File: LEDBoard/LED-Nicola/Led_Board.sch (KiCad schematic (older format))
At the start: 29 parts, among them J1 MOUNTING_HOLE, J10 CONN_01X02, J11 CONN_01X16, J12 CONN_01X02, J2 MOUNTING_HOLE, J3 MOUNTING_HOLE, J4 MOUNTING_HOLE, J5 CONN_01X04, J6 CONN_01X04, J7 CONN_01X02, J8 CONN_01X02, J9 CONN_01X02, Q1 MMBT2222ALT1G, U1 SSR

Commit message: Added changes as per Chris requests
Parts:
- removed J7: CONN_01X02, hyperCustom:CONN_PHOENIX_1844210_2PIN, symbol CONN_01X02
- added J13: LED CONN 01X04, hyperCustom:CONN_PHOENIX_1844236_4PIN, symbol CONN_01X04
- added J7: Arduino CONN_01X06, hyperCustom:CONN_PHOENIX_1844252_6PIN, symbol CONN_01X06
- added R15, R16, R17: 220, Resistors_SMD:R_1206_HandSoldering, symbol R
- J11: value CONN_01X16 -> LED CONN 01X16
- J5: value CONN_01X04 -> Arduino CONN 01X04
- J6: value CONN_01X04 -> Arduino CONN_01X04
- J8: value CONN_01X02 -> VD 0 CONN_01X02
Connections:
- net 24V: now also J5.3 (P3), U1.4 (SUPPLY2), U1.6 (SUPPLY1); no longer U1.1 (IN+)
- net A0: now also J5.2 (P2); no longer J5.4 (P4)
- net A1: now also J5.1 (P1); no longer J5.3 (P3)
- net A2: now also J6.4 (P4); no longer J5.2 (P2)
- net A3: now also J6.3 (P3); no longer J5.1 (P1)
- net A4: now also J6.2 (P2); no longer J6.4 (P4)
- net A5: now also J6.1 (P1); no longer J6.3 (P3)
- net A6: now also J7.6 (P6); no longer J6.2 (P2)
- net A7: now also J7.5 (P5), R15.2; no longer J6.1 (P1)
- net GND: now also J11.16 (P16), J13.2 (P2), J13.4 (P4), J7.2 (P2); no longer U1.2 (IN-)
- net Buzzer: now reaches U1.5 (LOAD)
- net Buzzer: now also J12.1 (P1)
- net L7: now reaches J11.15 (P15)
- net L7: now also R15.1
- net Collector: no longer names the net of Q1.3 (C)
- net Collector: now also U1.2 (IN-); no longer U1.6 (SUPPLY1)
- net LEDO renamed VDO0
- removed net buzzer: J12.1 (P1), U1.4 (SUPPLY2)
- new net 5V0: J5.4 (P4), U1.1 (IN+)
- new net A8: J7.4 (P4), R16.2
- new net A9: J7.3 (P3), R17.2
- new net L8: J13.1 (P1), R16.1
- new net L9: J13.3 (P3), R17.1
- no-connect marks 6 -> 3
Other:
- moved on the sheet: D1, J10, J11, J5, J6, J8, J9, Q1, R1, R10, R11, R12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

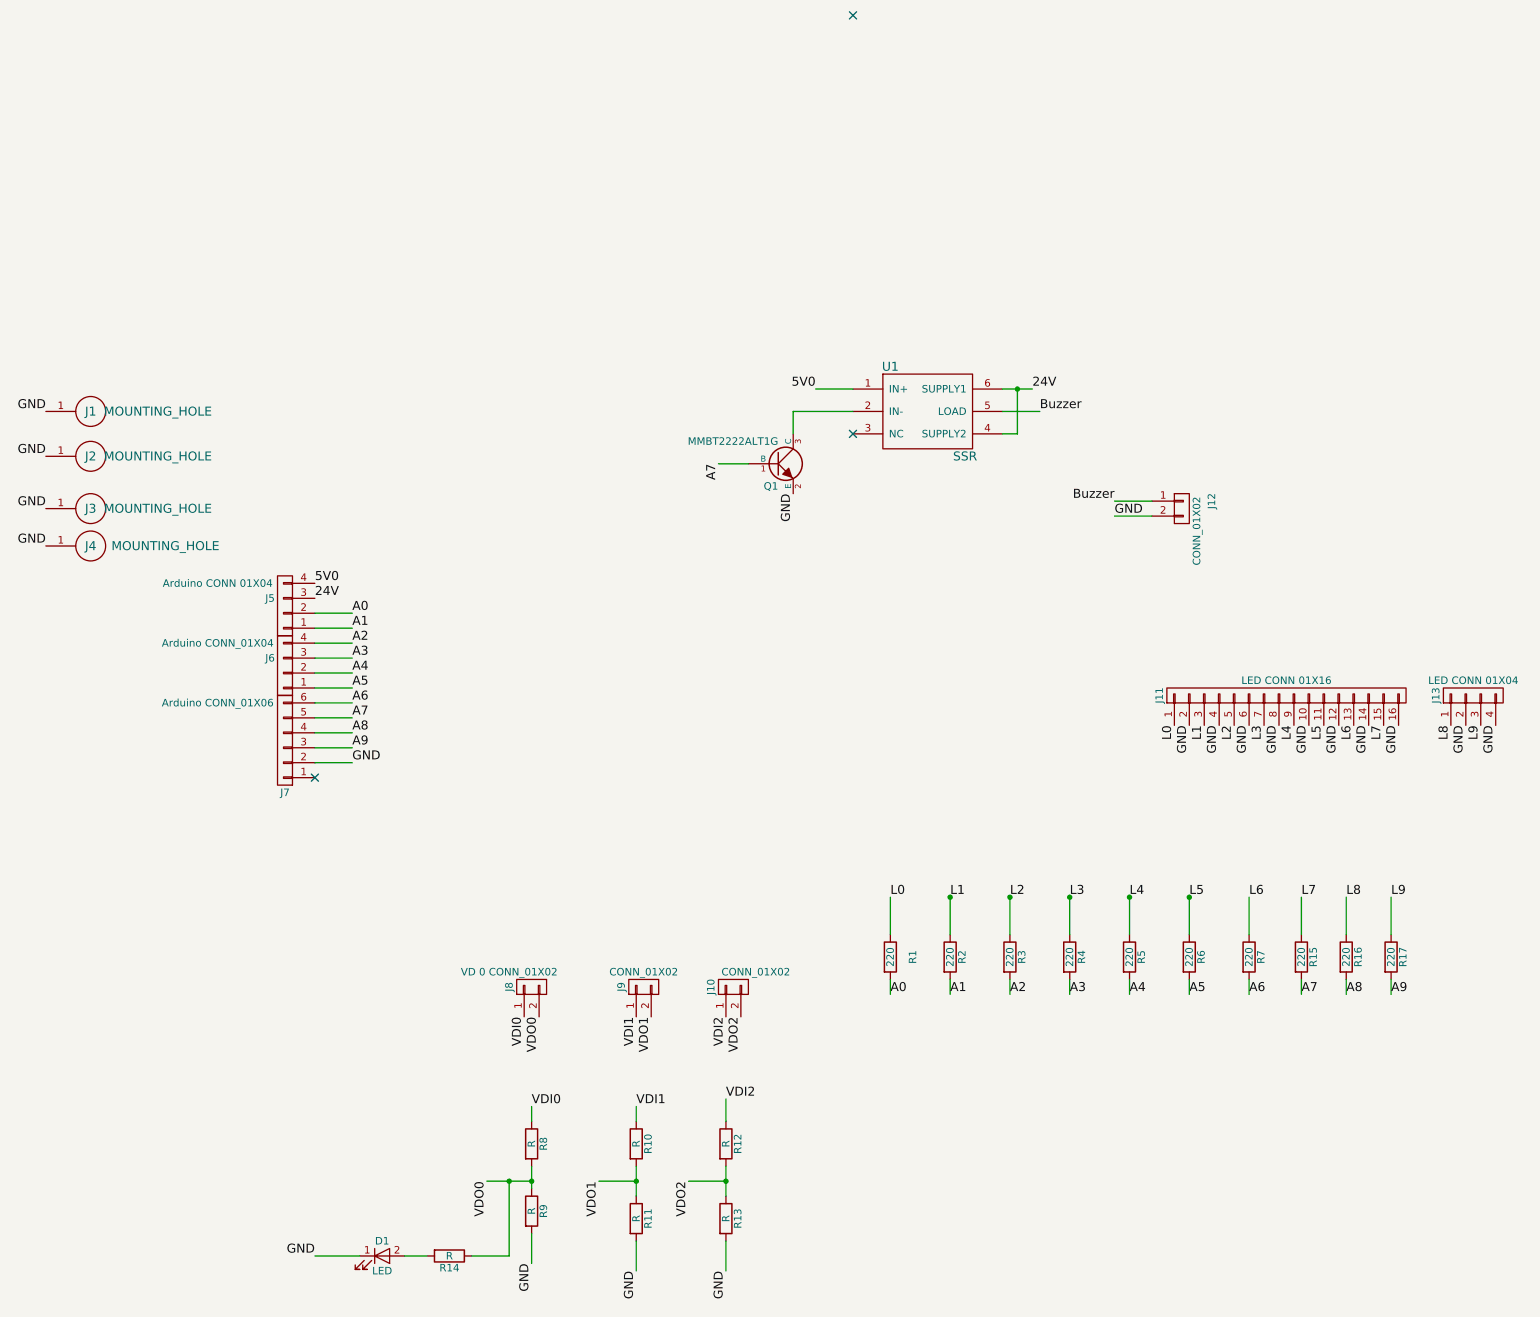
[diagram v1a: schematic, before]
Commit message: Added Digikey PN and Mfg. PN
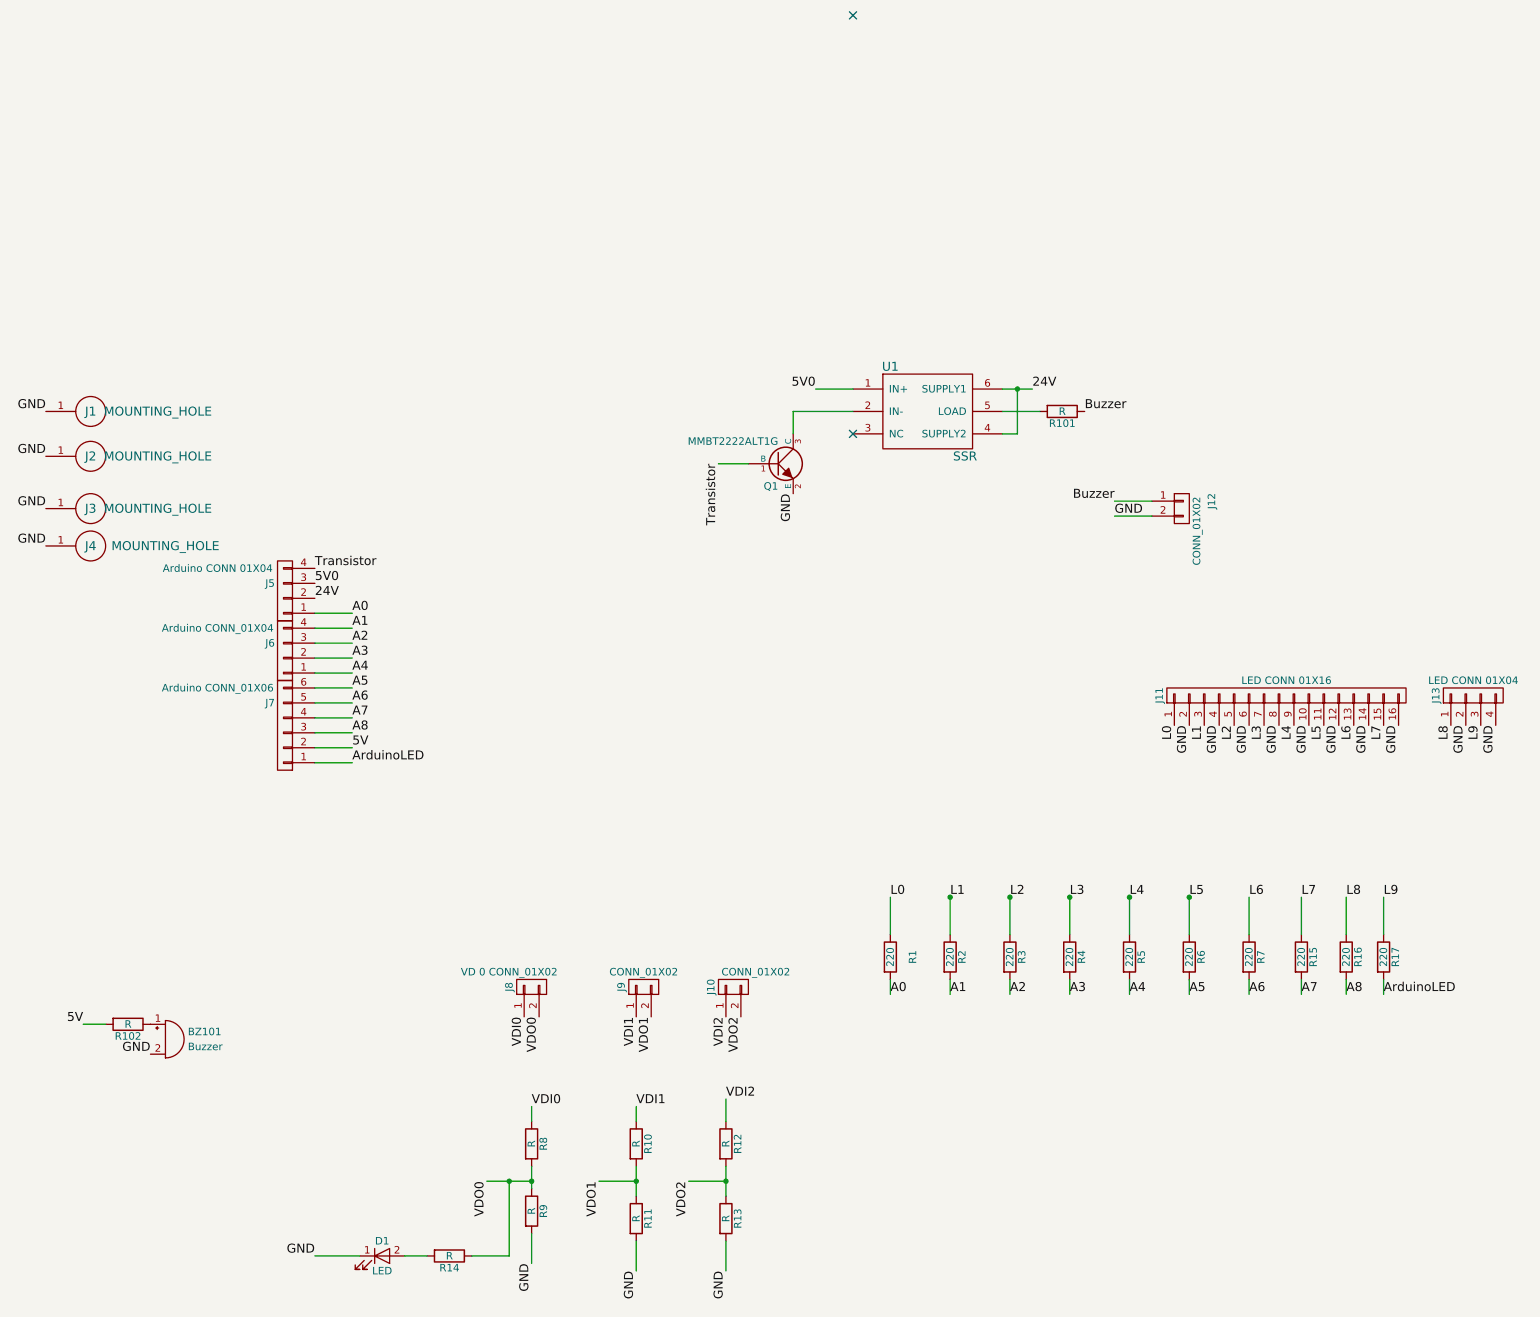
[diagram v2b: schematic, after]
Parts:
- added BZ101: Buzzer, hyperCustom:nicolaBuzzer, symbol Buzzer
- added R101, R102: R, Resistors_ThroughHole:R_Axial_DIN0309_L9.0mm_D3.2mm_P12.70mm_Horizontal, symbol R
- J10: DigiKey PN (none) -> 277-2416-ND; Mfg.  (none) -> Phoenix; Mfg. PN (none) -> 1844210
- J11: Digikey PN (none) -> 277-6211-ND; Link (none) -> https://www.digikey.com/product-detail/en/phoenix-contact/1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; Mfg.  (none) -> Phoenix; Mfg. PN (none) -> 1828003
- J12: Digikey PN (none) -> 277-2416-ND; Mfg.  (none) -> Phoenix; Mfg. PN (none) -> 1844210
- J13, J5, J6: Digikey PN (none) -> 277-2419-ND; Mfg.  (none) -> Phoenix; Mfg. PN (none) -> 1844236
- J7: Digikey PN (none) -> 277-2427-ND; Mfg.  (none) -> Phoenix; Mfg. PN (none) -> 1844525
- J8, J9: Digikey PN (none) -> 277-2416-ND; Mfg. (none) -> Phoenix; Mfg. PN (none) -> 1844210
- Q1: Mfg. (none) -> ON Semiconductors
- R1: Digikey PN (none) -> P.22RCT-ND; Mfg. (none) -> Panasonic Electronic Company; Mfg. Pn (none) -> ERJ-8RQFR22V
- R10, R11, R12, R13, R15, R2, R3, R5: Digikey PN (none) -> P.22RCT-ND; Mfg. (none) -> Panasonic Electronic Company; Mfg. PN (none) -> ERJ-8RQFR22V
- R14: Mfg. (none) -> Panasonic Electronic Company; Mfg. PN (none) -> ERJ-8RQFR22V; digikey PN (none) -> P.22RCT-ND
- R16: Digikey PN (none) -> P.22RCT-ND; Mfg PN (none) -> ERJ-8RQFR22V; Mfg. (none) -> Panasonic Electronic Company
- R17: Mfg. (none) -> Panasonic Electronic Company; Mfg. PN (none) -> ERJ-8RQFR22V; digikey PN  (none) -> P.22RCT-ND
- R4: DiIgkey PN (none) -> P.22RCT-ND; Mfg. (none) -> Panasonic Electronic Company; Mfg. PN (none) -> ERJ-8RQFR22V
- R6: Mfg. (none) -> Panasonic Electronic Company; Mfg. PN (none) -> ERJ-8RQFR22V
- R7: Digi key PN (none) -> P.22RCT-ND; Mfg. (none) -> Panasonic Electronic Company; Mfg. PN (none) -> ERJ-8RQFR22V
- R8: DigiKey PN (none) -> P3-9PCT-ND; Mfg. (none) -> Panasonic Electronic Company; Mfg. PN (none) -> ERJ-8RQJ3R9V
- R9: Digi Key PN (none) -> P17633CT-ND; Mfg. (none) -> Panasonic Electronic Company; Mfg. PN (none) -> ERJ-8QFR62V
- U1: Digikey PN (none) -> VO14642AABCT-ND; Mfg (none) -> Vishay Semiconductor Oppto Division; Mfg. PN (none) -> VO14642AABTR
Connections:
- net 24V: now also J5.2 (P2); no longer J5.3 (P3)
- net 5V0: now also J5.3 (P3); no longer J5.4 (P4)
- net A0: now also J5.1 (P1); no longer J5.2 (P2)
- net A1: now also J6.4 (P4); no longer J5.1 (P1)
- net A2: now also J6.3 (P3); no longer J6.4 (P4)
- net A3: now also J6.2 (P2); no longer J6.3 (P3)
- net A4: now also J6.1 (P1); no longer J6.2 (P2)
- net A5: now also J7.6 (P6); no longer J6.1 (P1)
- net A6: now also J7.5 (P5); no longer J7.6 (P6)
- net A7: now also J7.4 (P4); no longer J7.5 (P5), Q1.1 (B)
- net A8: now also J7.3 (P3); no longer J7.4 (P4)
- net Buzzer: now also R101.1; no longer U1.5 (LOAD)
- net GND: now also BZ101.2 (+); no longer J7.2 (P2)
- net ArduinoLED: now reaches J7.1 (P1)
- net ArduinoLED: now also R17.2
- removed net A9: J7.3 (P3), R17.2
- new net: R101.2, U1.5 (LOAD)
- new net: BZ101.1 (-), R102.1
- new net 5V: J7.2 (P2), R102.2
- new net Transistor: J5.4 (P4), Q1.1 (B)
- no-connect marks 3 -> 2
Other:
- moved on the sheet: J5, J6, J7
